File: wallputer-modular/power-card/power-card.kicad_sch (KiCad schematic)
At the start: 174 parts, among them J2 Power, Q1 FQP27P06, Q2 IRLZ44N, SW1 reset, U1 NE555P, U12 74HC04, U16 74HC04, U17 74HC04, U18 74HC04, U2 74HC04, U3 74HC04

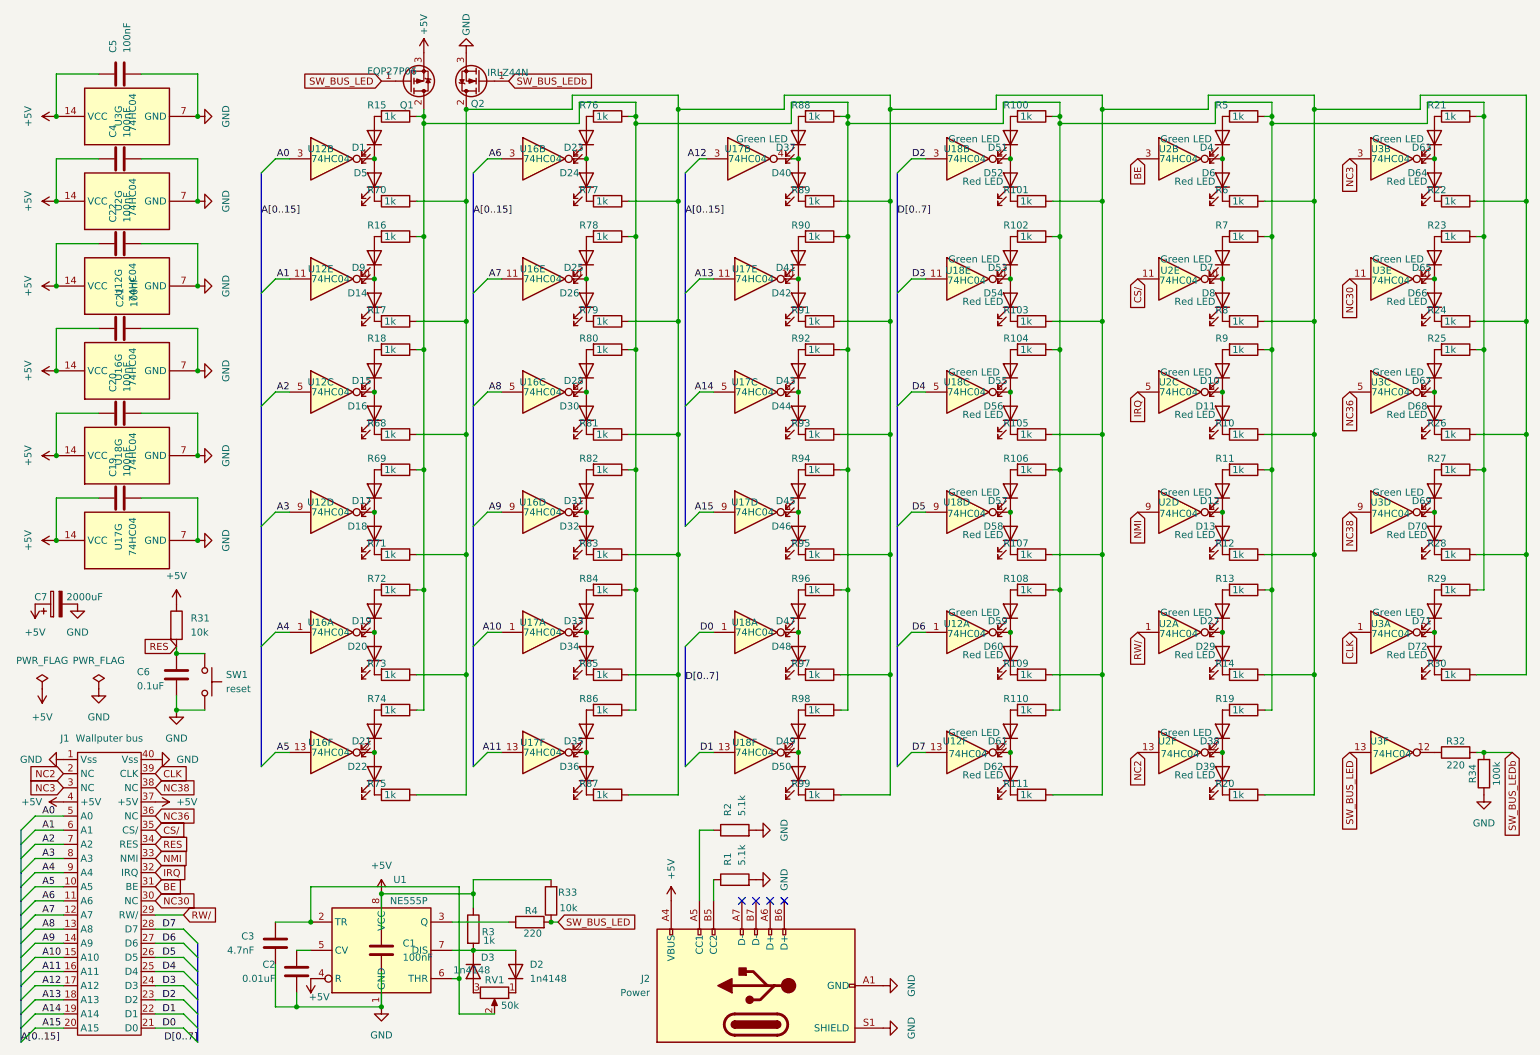
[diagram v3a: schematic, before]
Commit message: begin wiring pcb
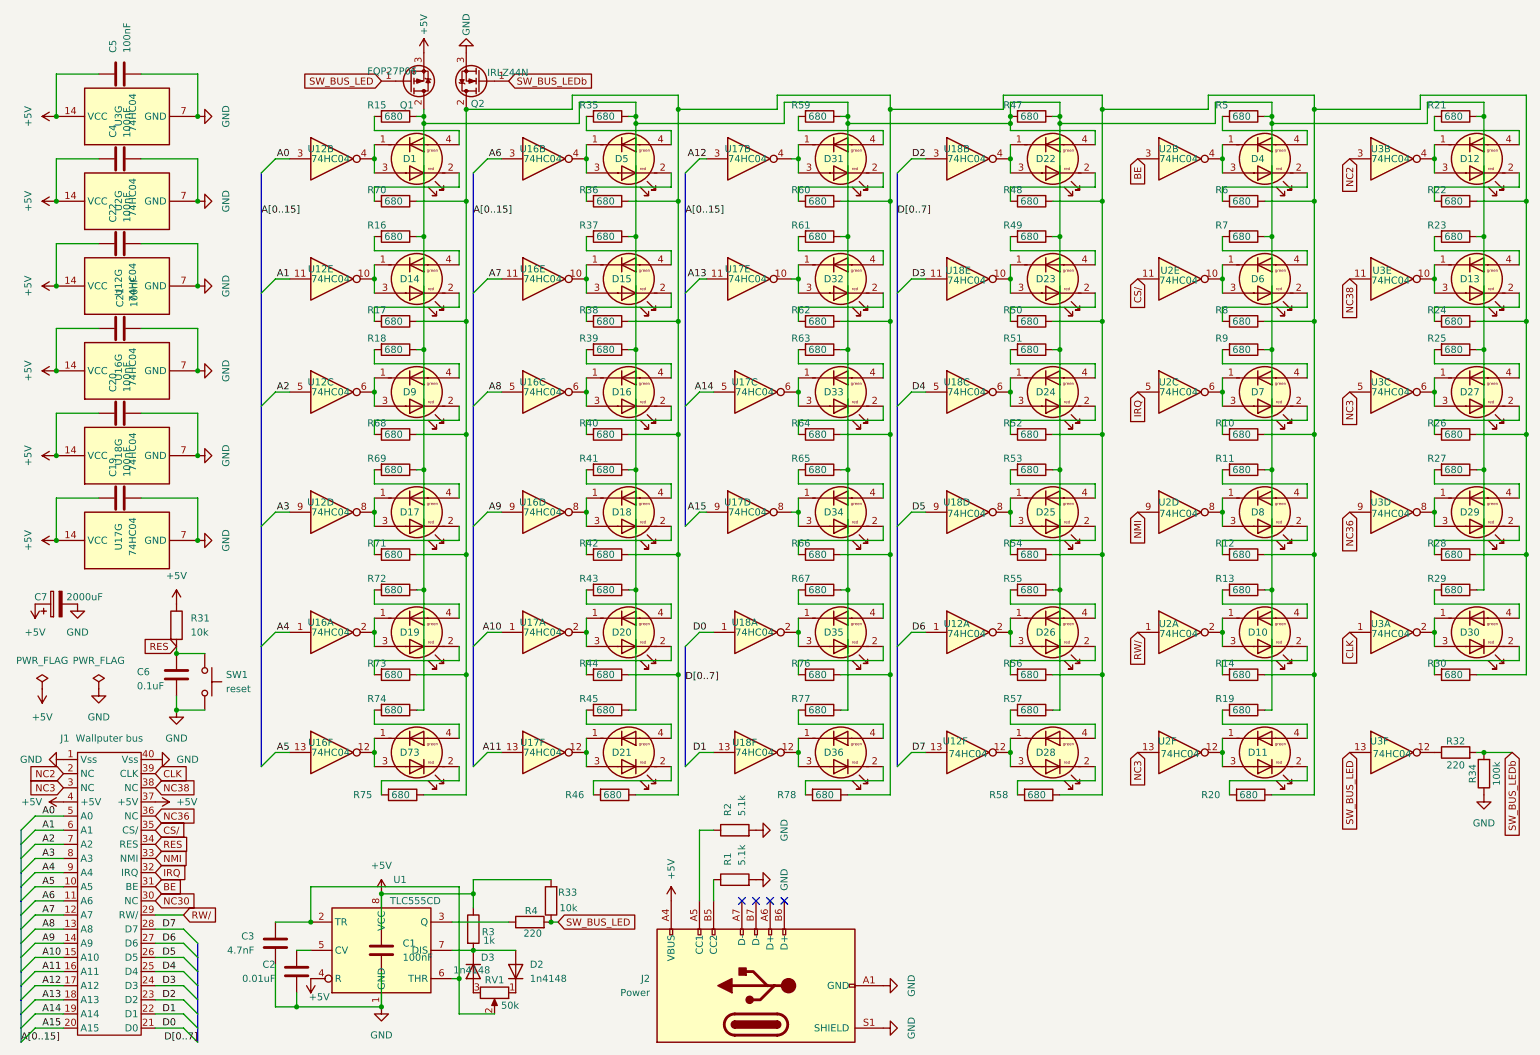
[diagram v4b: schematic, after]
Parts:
- removed D1, D10, D12, D15, D17, D19, D21, D23, D25, D27, D28, D31, D33, D35, D37, D38, D4, D41, D43, D45, D47, D49, D51, D53, D55, D57, D59, D61, D63, D65, D67, D69, D7, D71, D9: Green LED, LED_THT:LED_D3.0mm, symbol Device:LED
- removed D11, D13, D14, D16, D18, D20, D22, D24, D26, D29, D30, D32, D34, D36, D39, D40, D42, D44, D46, D48, D5, D50, D52, D54, D56, D58, D6, D60, D62, D64, D66, D68, D70, D72, D8: Red LED, LED_THT:LED_D3.0mm, symbol Device:LED
- removed R100, R101, R102, R103, R104, R105, R106, R107, R108, R109, R110, R111, R79, R80, R81, R82, R83, R84, R85, R86, R87, R88, R89, R90, R91, R92, R93, R94, R95, R96, R97, R98, R99: 1k, Resistor_THT:R_Axial_DIN0204_L3.6mm_D1.6mm_P2.54mm_Vertical, symbol Device:R
- added D1, D10, D11, D12, D13, D14, D15, D16, D17, D18, D19, D20, D21, D22, D23, D24, D25, D26, D27, D28, D29, D30, D31, D32, D33, D34, D35, D36, D4, D5, D6, D7, D73, D8, D9: Wallputer_Dual_LED, Wallputer:Wallputer_Dual_LED, symbol Wallputer:Wallputer_Dual_LED
- added R35, R36, R37, R38, R39, R40, R41, R42, R43, R44, R45, R46, R47, R48, R49, R50, R51, R52, R53, R54, R55, R56, R57, R58, R59, R60, R61, R62, R63, R64, R65, R66, R67: 680, Resistor_SMD:R_0603_1608Metric, symbol Device:R
- J1: footprint Wallputer:Wallputer_Bus_Socket -> Wallputer:Wallputer_Bus_*
- R10, R11, R12, R13, R14, R15, R16, R17, R18, R19, R20, R21, R22, R23, R24, R25, R26, R27, R28, R29, R30, R5, R6, R68, R69, R7, R70, R71, R72, R73, R74, R75, R76, R77, R78, R8, R9: value 1k -> 680; footprint Resistor_THT:R_Axial_DIN0204_L3.6mm_D1.6mm_P2.54mm_Vertical -> Resistor_SMD:R_0603_1608Metric
- U1: value NE555P -> TLC555CD
- U12, U16, U17, U18, U2, U3: footprint Package_DIP:DIP-14_W7.62mm_Socket -> Package_SO:SO-14_3.9x8.65mm_P1.27mm
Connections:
- net NC2: now also U3.3; no longer U2.13
- net NC3: now also U2.13, U3.5; no longer U3.3
- net NC30: no longer U3.11
- net NC36: now also U3.9; no longer U3.5
- net NC38: now also U3.11; no longer U3.9
- net at U16.10: now also D15.1 (Green_A), D15.3 (Red_K)
- net at U17.12: now also D21.1 (Green_A), D21.3 (Red_K)
- net at U12.4: now also D1.1 (Green_A), D1.3 (Red_K)
- net at U12.10: now also D14.1 (Green_A), D14.3 (Red_K)
- net at R16.2: now also D14.4 (Green_K)
- net at U3.4: now also D12.1 (Green_A), D12.3 (Red_K)
- net at R21.2: now also D12.4 (Green_K)
- net at R8.2: now also D6.2 (Red_A)
- net at U2.10: now also D6.1 (Green_A), D6.3 (Red_K)
- net at Q2.2 (D), R10.1, R12.1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: now also R76.1, R78.1, R36.1, R38.1, R40.1, R42.1, R44.1, R46.1, R48.1, R50.1, R52.1, R54.1, R56.1, R58.1, R60.1, R62.1, R64.1, R66.1; no longer R77.1
- net at U17.4: now also D31.1 (Green_A), D31.3 (Red_K)
- net at R22.2: now also D12.2 (Red_A)
- net at Q1.2 (D), R11.1, R13.1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: now also R77.1, D22.4 (Green_K), R35.1, R37.1, R39.1, R41.1, R43.1, R45.1, R47.1, R47.2, R49.1, R51.1, R53.1, R55.1, R57.1, R59.1, R61.1, R63.1, R65.1, R67.1; no longer R76.1, R78.1
- net at R68.2: now also D9.2 (Red_A)
- net at U12.6: now also D9.1 (Green_A), D9.3 (Red_K)
- net at R20.2: now also D11.2 (Red_A)
- net at U2.12: now also D11.1 (Green_A), D11.3 (Red_K)
- net at U17.6: now also D33.1 (Green_A), D33.3 (Red_K)
- net at R15.2: now also D1.4 (Green_K)
- net at U2.2: now also D10.1 (Green_A), D10.3 (Red_K)
- net at U18.2: now also D35.1 (Green_A), D35.3 (Red_K)
- net at U17.10: now also D32.1 (Green_A), D32.3 (Red_K)
- net at R77.2: now also D36.4 (Green_K)
- net at U16.4: now also D5.1 (Green_A), D5.3 (Red_K)
- net at U18.6: now also D24.1 (Green_A), D24.3 (Red_K)
- net at R76.2: now also D35.2 (Red_A)
- net at R13.2: now also D10.4 (Green_K)
- net at R78.2: now also D36.2 (Red_A)
- net at U16.8: now also D18.1 (Green_A), D18.3 (Red_K)
- net at R75.2: now also D73.2 (Red_A)
- net at U2.8: now also D8.1 (Green_A), D8.3 (Red_K)
- net at R11.2: now also D8.4 (Green_K)
- net at U3.10: now also D13.1 (Green_A), D13.3 (Red_K)
- net at R23.2: now also D13.4 (Green_K)
- net at U18.4: now also D22.1 (Green_A), D22.3 (Red_K)
- net at R12.2: now also D8.2 (Red_A)
- net at R71.2: now also D17.2 (Red_A)
- net at U12.8: now also D17.1 (Green_A), D17.3 (Red_K)
- net at U12.2: now also D26.1 (Green_A), D26.3 (Red_K)
- net at U18.10: now also D23.1 (Green_A), D23.3 (Red_K)
- net at R74.2: now also D73.4 (Green_K)
- net at U18.12: now also D36.1 (Green_A), D36.3 (Red_K)
- net at R69.2: now also D17.4 (Green_K)
- net at R14.2: now also D10.2 (Red_A)
- net at U16.6: now also D16.1 (Green_A), D16.3 (Red_K)
- net at R30.2: now also D30.2 (Red_A)
- net at U3.2: now also D30.1 (Green_A), D30.3 (Red_K)
- net at R24.2: now also D13.2 (Red_A)
- net at U16.12: now also D73.1 (Green_A), D73.3 (Red_K)
- net at R18.2: now also D9.4 (Green_K)
- net at R70.2: now also D1.2 (Red_A)
- net at U17.2: now also D20.1 (Green_A), D20.3 (Red_K)
- net at U2.6: now also D7.1 (Green_A), D7.3 (Red_K)
- net at R9.2: now also D7.4 (Green_K)
- net at R19.2: now also D11.4 (Green_K)
- net at U18.8: now also D25.1 (Green_A), D25.3 (Red_K)
- net at R73.2: now also D19.2 (Red_A)
- net at U16.2: now also D19.1 (Green_A), D19.3 (Red_K)
- net at R26.2: now also D27.2 (Red_A)
- net at U17.8: now also D34.1 (Green_A), D34.3 (Red_K)
- net at U12.12: now also D28.1 (Green_A), D28.3 (Red_K)
- net at R29.2: now also D30.4 (Green_K)
- net at R17.2: now also D14.2 (Red_A)
- net at U3.6: now also D27.1 (Green_A), D27.3 (Red_K)
- net at R25.2: now also D27.4 (Green_K)
- net at R6.2: now also D4.2 (Red_A)
- net at U2.4: now also D4.1 (Green_A), D4.3 (Red_K)
- net at U3.8: now also D29.1 (Green_A), D29.3 (Red_K)
- net at R27.2: now also D29.4 (Green_K)
- net at R28.2: now also D29.2 (Red_A)
- net at R5.2: now also D4.4 (Green_K)
- net at R7.2: now also D6.4 (Green_K)
- net at R72.2: now also D19.4 (Green_K)
- net at R10.2: now also D7.2 (Red_A)
- new net: D23.2 (Red_A), R50.2
- new net: D28.2 (Red_A), R58.2
- new net: D33.2 (Red_A), R64.2
- new net: D24.4 (Green_K), R51.2
- new net: D28.4 (Green_K), R57.2
- new net: D34.4 (Green_K), R65.2
- new net: D26.4 (Green_K), R55.2
- new net: D21.2 (Red_A), R46.2
- new net: D21.4 (Green_K), R45.2
- new net: D5.2 (Red_A), R36.2
- new net: D33.4 (Green_K), R63.2
- new net: D15.2 (Red_A), R38.2
- new net: D25.4 (Green_K), R53.2
- new net: D34.2 (Red_A), R66.2
- new net: D20.2 (Red_A), R44.2
- new net: D31.4 (Green_K), R59.2
- new net: D16.2 (Red_A), R40.2
- new net: D16.4 (Green_K), R39.2
- new net: D23.4 (Green_K), R49.2
- new net: D25.2 (Red_A), R54.2
- new net: D31.2 (Red_A), R60.2
- new net: D22.2 (Red_A), R48.2
- new net: D35.4 (Green_K), R67.2
- new net: D15.4 (Green_K), R37.2
- new net: D24.2 (Red_A), R52.2
- new net: D5.4 (Green_K), R35.2
- new net: D32.2 (Red_A), R62.2
- new net: D26.2 (Red_A), R56.2
- new net: D18.2 (Red_A), R42.2
- new net: D32.4 (Green_K), R61.2
- new net: D18.4 (Green_K), R41.2
- new net: D20.4 (Green_K), R43.2
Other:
- moved on the sheet: R75, U17D, U17E

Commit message: More layout
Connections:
- net at Q1.2 (D), R11.1, R13.1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: no longer D22.4 (Green_K), R47.2
- new net: D22.4 (Green_K), R47.2
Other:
- moved on the sheet: R47
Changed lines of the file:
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@@
 	)
 	(junction
-		(at 190.5 30.48)
-		(diameter 0)
-		(color 0 0 0 0)
-	)
-	(junction
 		(at 161.29 72.39)
 		(diameter 0)
@@
 	)
 	(junction
-		(at 190.5 31.75)
-		(diameter 0)
-		(color 0 0 0 0)
-	)
-	(junction
 		(at 92.71 130.81)
 		(diameter 0)
@@
 	(wire
 		(pts
-			(xy 190.5 31.75) (xy 190.5 30.48)
+			(xy 190.5 27.94) (xy 190.5 31.75)
 		)
 		(stroke
@@
 	(wire
 		(pts
-			(xy 199.39 30.48) (xy 198.12 30.48)
-		)
-		(stroke
-			(width 0)
-			(type default)
-		)
-	)
-	(wire
-		(pts
 			(xy 190.5 142.24) (xy 190.5 144.78)
 		)
@@
 	(wire
 		(pts
-			(xy 190.5 30.48) (xy 190.5 27.94)
-		)
-		(stroke
-			(width 0)
-			(type default)
-		)
-	)
-	(wire
-		(pts
 			(xy 85.09 52.07) (xy 83.82 52.07)
 		)
@@
 	(wire
 		(pts
-			(xy 190.5 33.02) (xy 190.5 31.75)
-		)
-		(stroke
-			(width 0)
-			(type default)
-		)
-	)
-	(wire
-		(pts
 			(xy 161.29 152.4) (xy 168.91 152.4)
 		)
@@
 	(wire
 		(pts
-			(xy 205.74 33.02) (xy 190.5 33.02)
+			(xy 205.74 33.02) (xy 191.77 33.02)
 		)
 		(stroke
@@
 	(wire
 		(pts
+			(xy 191.77 30.48) (xy 191.77 33.02)
+		)
+		(stroke
+			(width 0)
+			(type default)
+		)
+	)
+	(wire
+		(pts
 			(xy 96.52 101.6) (xy 99.06 101.6)
 		)
@@
 	(symbol
 		(lib_id "Device:R")
-		(at 194.31 30.48 270)
+		(at 195.58 30.48 270)
 		(unit 1)
 		(exclude_from_sim no)
@@
 		(dnp no)
 		(property "Reference" "R47"
-			(at 189.23 28.448 90)
+			(at 190.5 28.448 90)
 			(effects
 				(font
@@
 		)
 		(property "Value" "680"
-			(at 192.278 30.48 90)
+			(at 194.056 30.48 90)
 			(effects
 				(font
@@
 		)
 		(property "Footprint" "Resistor_SMD:R_0603_1608Metric"
-			(at 194.31 28.702 90)
+			(at 195.58 28.702 90)
 			(effects
 				(font
@@
 		)
 		(property "Datasheet" "~"
-			(at 194.31 30.48 0)
+			(at 195.58 30.48 0)
 			(effects
 				(font
@@
 		)
 		(property "Description" "Resistor"
-			(at 194.31 30.48 0)
+			(at 195.58 30.48 0)
 			(effects
 				(font

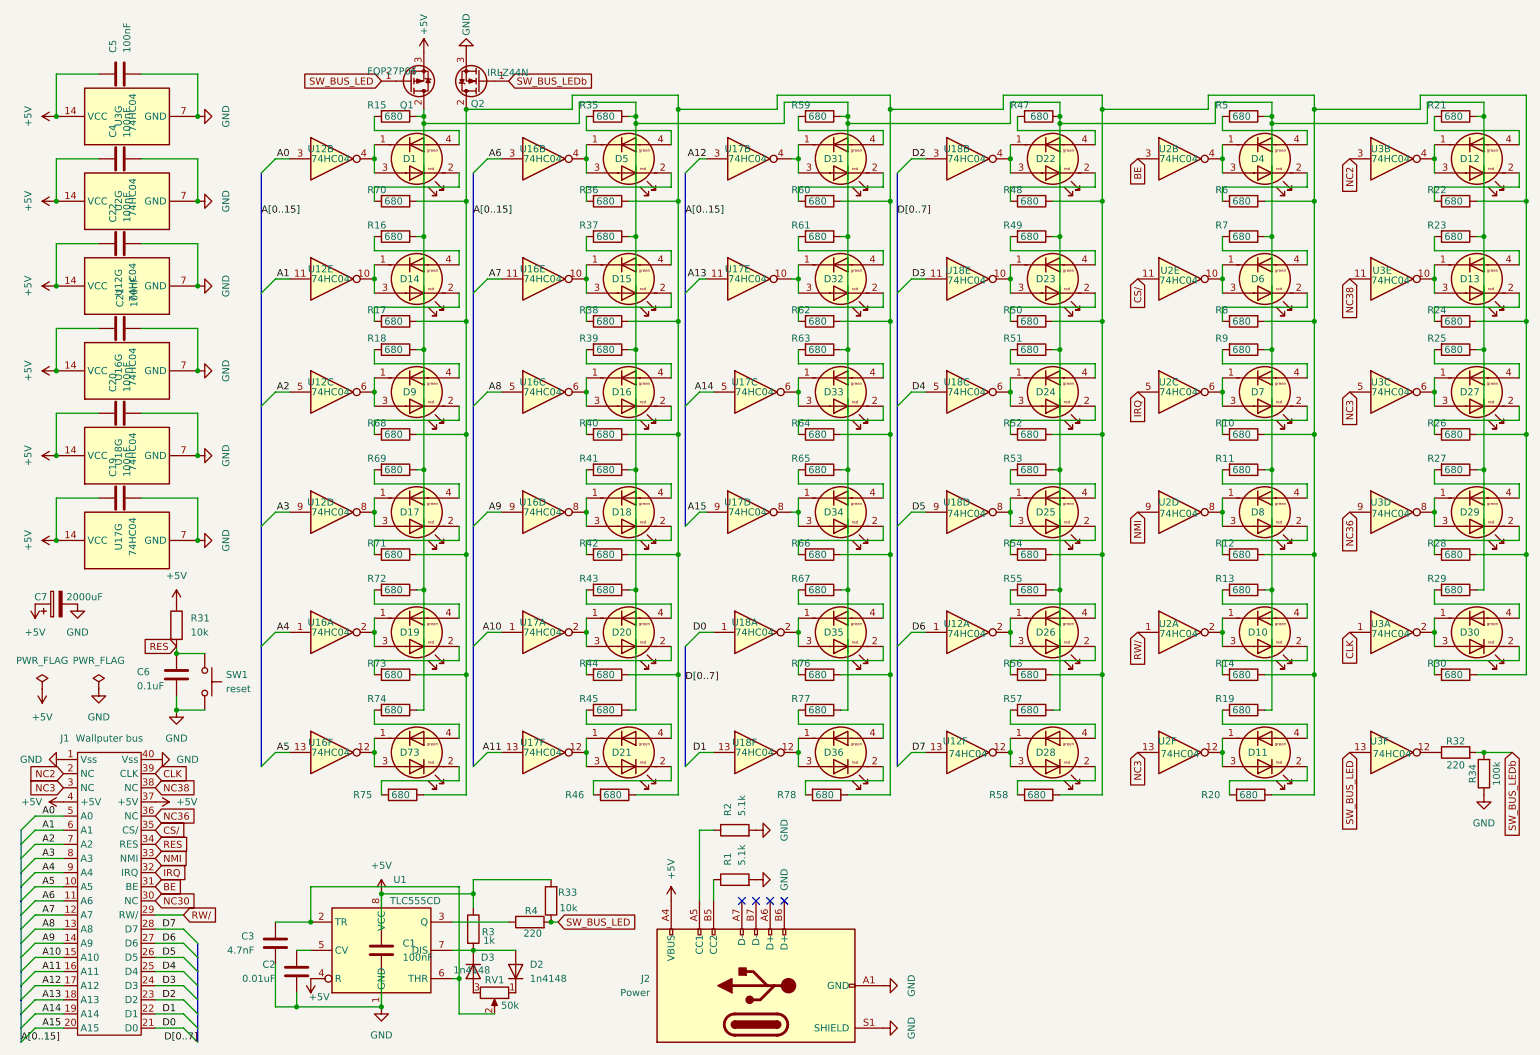
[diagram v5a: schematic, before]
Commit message: finish wiring pcb
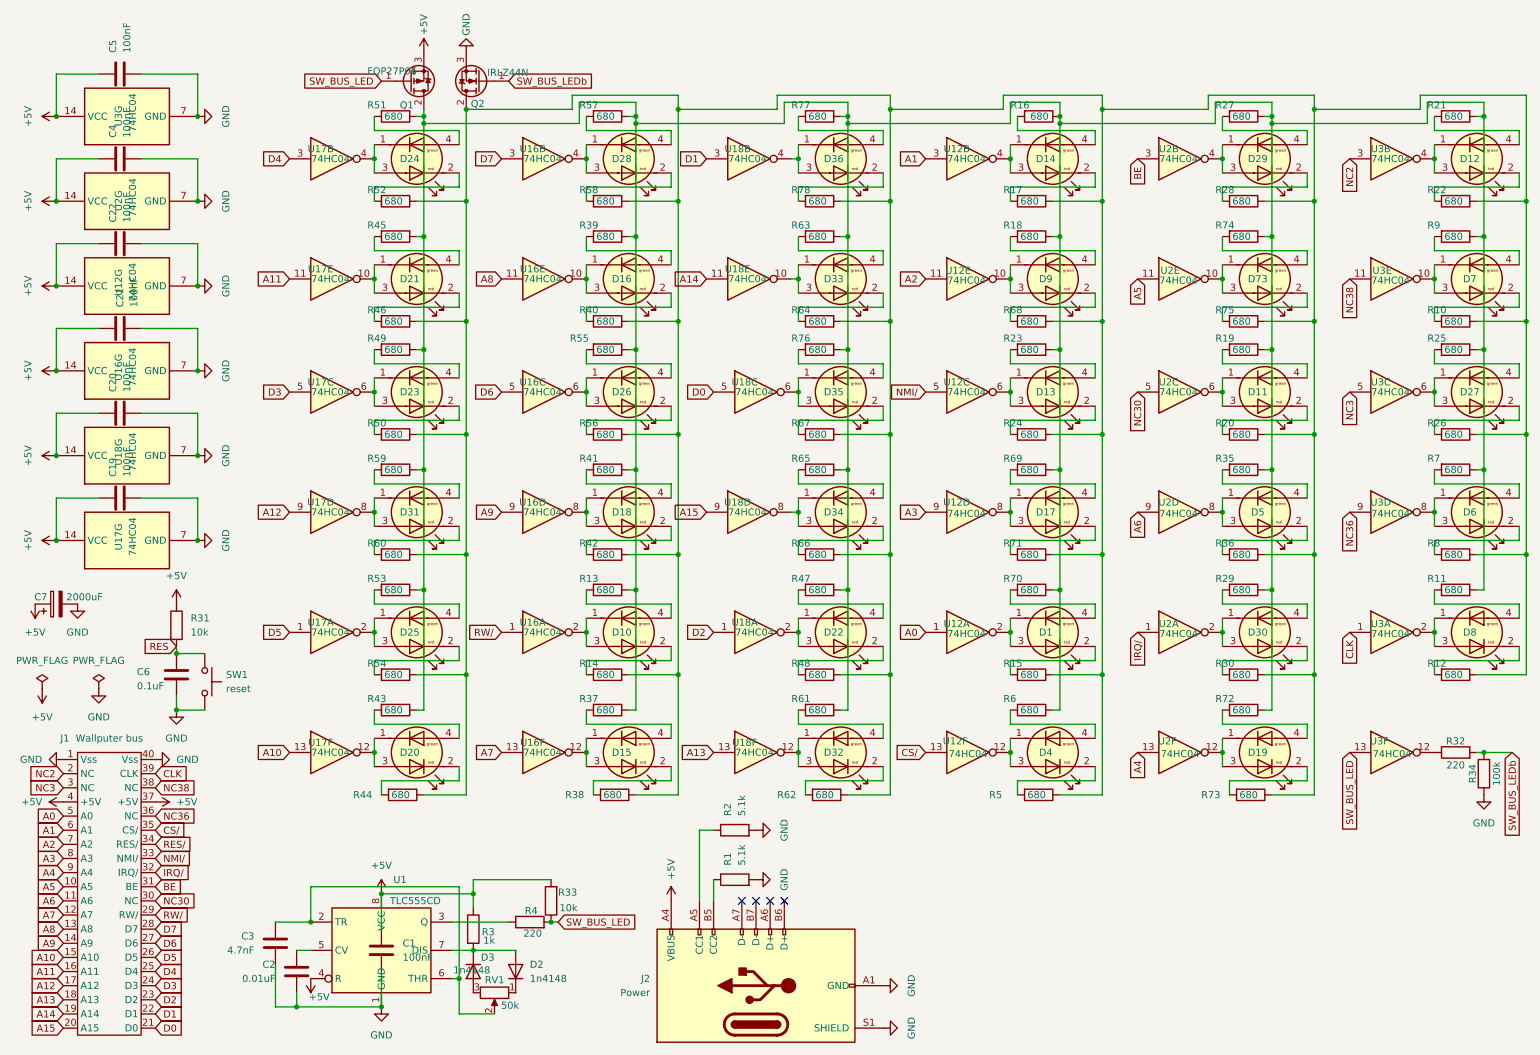
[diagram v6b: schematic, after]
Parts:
- renumbered D26 to D1, D20 to D10, D7 to D11, D24 to D13, D22 to D14, D21 to D15, D15 to D16, D25 to D17, D11 to D19, D73 to D20, D14 to D21, D35 to D22, D9 to D23, D1 to D24, D19 to D25, D16 to D26, D5 to D28, D4 to D29, D10 to D30, D17 to D31, D36 to D32, D32 to D33, D33 to D35, D31 to D36, D28 to D4, D8 to D5, D29 to D6, D13 to D7, D6 to D73, D30 to D8, D23 to D9, R24 to R10, R29 to R11, R30 to R12, R43 to R13, R44 to R14, R56 to R15, R47 to R16, R48 to R17, R49 to R18, R9 to R19, R10 to R20, R51 to R23, R52 to R24, R5 to R27, R6 to R28, R13 to R29, R14 to R30, R11 to R35, R12 to R36, R45 to R37, R46 to R38, R37 to R39, R38 to R40, R74 to R43, R75 to R44, R16 to R45, R17 to R46, R67 to R47, R76 to R48, R18 to R49, R58 to R5, R68 to R50, R15 to R51, R70 to R52, R72 to R53, R73 to R54, R39 to R55, R40 to R56, R35 to R57, R36 to R58, R69 to R59, R57 to R6, R71 to R60, R77 to R61, R78 to R62, R61 to R63, R62 to R64, R64 to R67, R50 to R68, R53 to R69, R27 to R7, R55 to R70, R54 to R71, R19 to R72, R20 to R73, R7 to R74, R8 to R75, R63 to R76, R59 to R77, R60 to R78, R28 to R8, R23 to R9, U18 to U12, U17 to U16, U12 to U17, U16 to U17, U17 to U18
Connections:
- net A0: now also U12.1; no longer U17.3
- net A1: now also U12.3; no longer U17.11
- net A10: now also U17.13; no longer U16.1
- net A11: now also U17.11; no longer U16.13
- net A12: now also U17.9; no longer U18.3
- net A13: now also U18.13; no longer U18.11
- net A14: now also U18.11; no longer U18.5
- net A2: now also U12.11; no longer U17.5
- net A3: now also U12.9; no longer U17.9
- net A4: now also U2.13; no longer U17.1
- net A5: now also U2.11; no longer U17.13
- net A6: now also U2.9; no longer U16.3
- net A7: now also U16.13; no longer U16.11
- net A8: now also U16.11; no longer U16.5
- net CS/: now also U12.13; no longer U2.11
- net D0: now also U18.5; no longer U18.1
- net D1: now also U18.3; no longer U18.13
- net D2: now also U18.1; no longer U12.3
- net D3: now also U17.5; no longer U12.11
- net D4: now also U17.3; no longer U12.5
- net D5: now also U17.1; no longer U12.9
- net D6: now also U16.5; no longer U12.1
- net D7: now also U16.3; no longer U12.13
- net NC3: no longer U2.13
- net NC30: now also U2.5
- net RES: no longer J1.34 (RES)
- net RW/: now also U16.1; no longer U2.1
- net IRQ renamed IRQ/
- net IRQ/: now also U2.1; no longer U2.5
- net NMI renamed NMI/
- net NMI/: now also U12.5; no longer U2.9
- new net RES/: J1.34 (RES/)
